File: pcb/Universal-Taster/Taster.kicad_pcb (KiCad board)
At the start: 2 copper layers, 30 x 30 mm, 59 parts, among them J1 I2C, J2 INTERFACE, J3 KNX_KLEMME, J4 JTAG, SW1 PROG, U1 EFM32PG12B500, U2 NCN5121, U3 MX25R8035F, Y1 32.768kHz, Y2 40MHz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

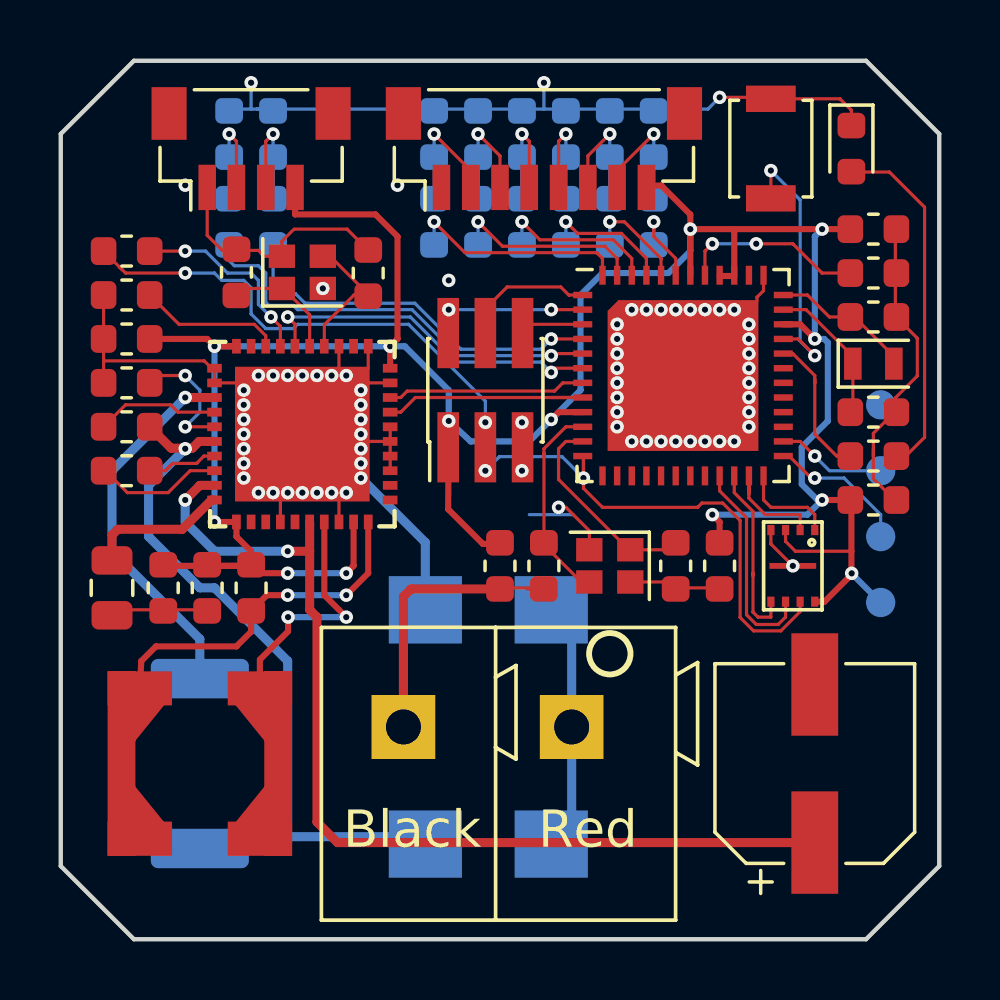
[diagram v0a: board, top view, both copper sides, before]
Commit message: Version 1.2.1 of Universal-Taster
- More clearance of traces around resistor SCL line
- Fixed DRC errors (new in Kicad 5.1.x)
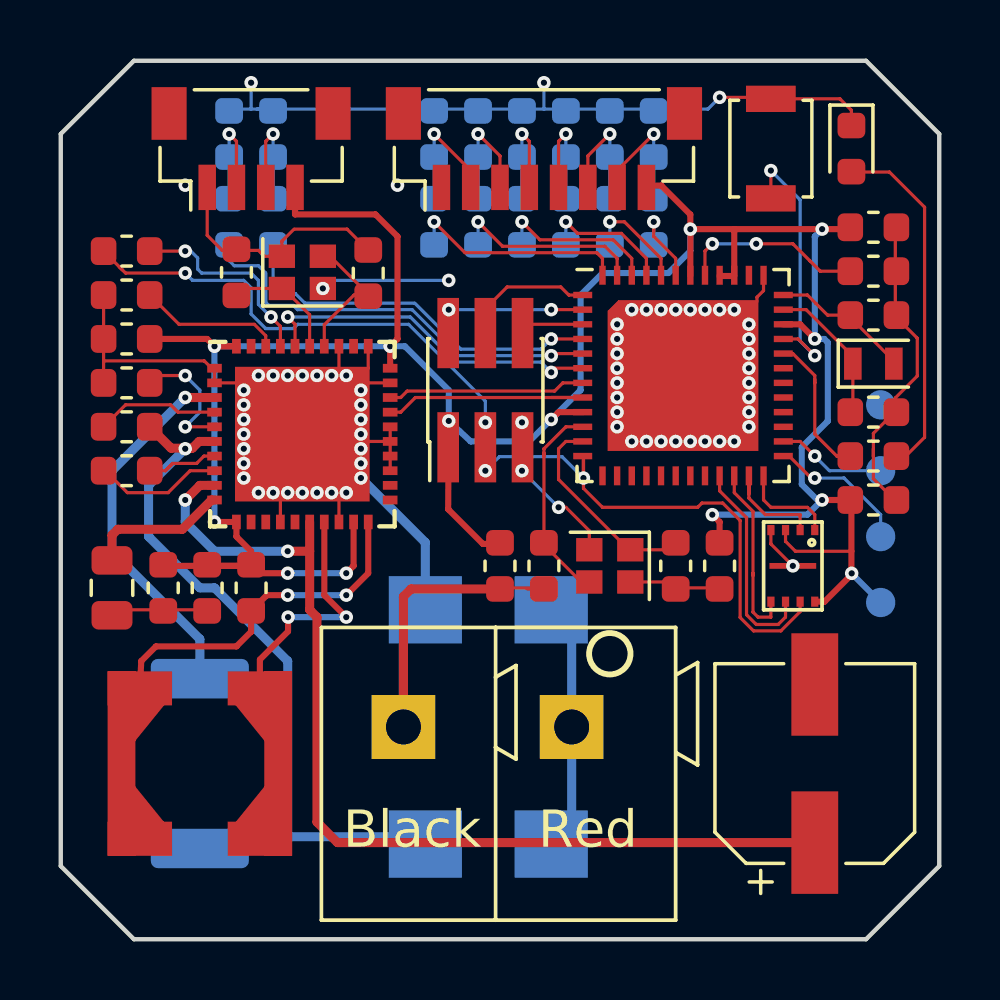
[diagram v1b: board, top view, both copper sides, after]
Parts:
- moved C2 0.06 mm to (97.8, 48.7)
- moved C3 0.06 mm to (97.8, 47.2)
- moved C8 0.06 mm to (97.8, 45.7)
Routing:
- net GND: track 137.9 -> 142.6 mm
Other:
- board text added: "BasilFX 07/2021 V1.2.1"
- board text removed: "BasilFX 08/2018 V1.2.0"
